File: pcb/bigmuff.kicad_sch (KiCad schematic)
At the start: 62 parts, among them J1 NRJ4HF, J10 Conn_01x02_Pin, J11 Conn_01x02_Pin, J2 NRJ4HF, J3 Conn_01x02_Pin, J4 Barrel_Jack_Switch, J5 Conn_01x02_Pin, J6 Conn_01x02_Pin, J7 Conn_01x02_Pin, J8 Conn_01x02_Pin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

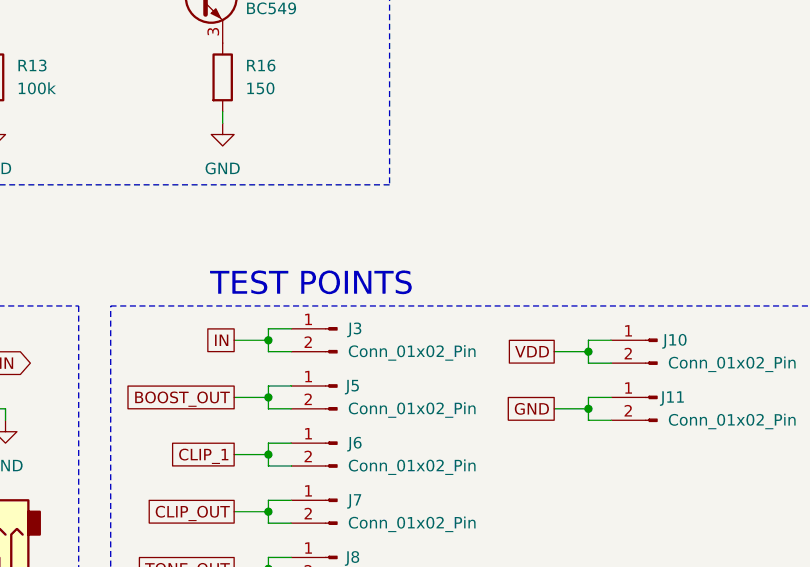
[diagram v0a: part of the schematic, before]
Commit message: added 3d models
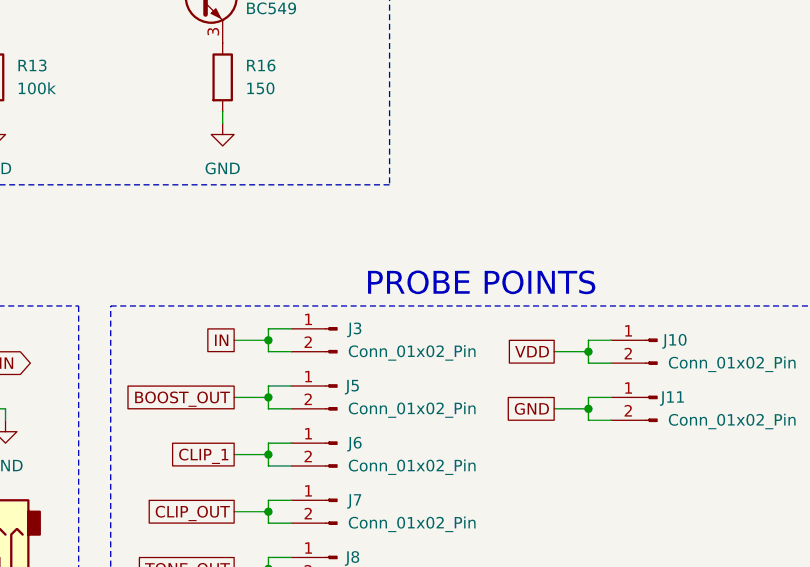
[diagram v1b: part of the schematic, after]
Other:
- note added: "PROBE POINTS"
- note removed: "TEST POINTS"
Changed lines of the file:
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@@
 		)
 	)
-	(text "TEST POINTS"
+	(text "PROBE POINTS"
 		(exclude_from_sim no)
-		(at 216.916 103.124 0)
+		(at 235.712 103.124 0)
 		(effects
 			(font

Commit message: Passed ERC / DRC - ready for gerbers
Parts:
- added H1, H2, H3, H4: MountingHole, MountingHole:MountingHole_3.2mm_M3, symbol Mechanical:MountingHole
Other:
- note added: "MOUNTING"
- moved on the sheet: J10, J11
